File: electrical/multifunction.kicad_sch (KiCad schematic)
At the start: 19 parts

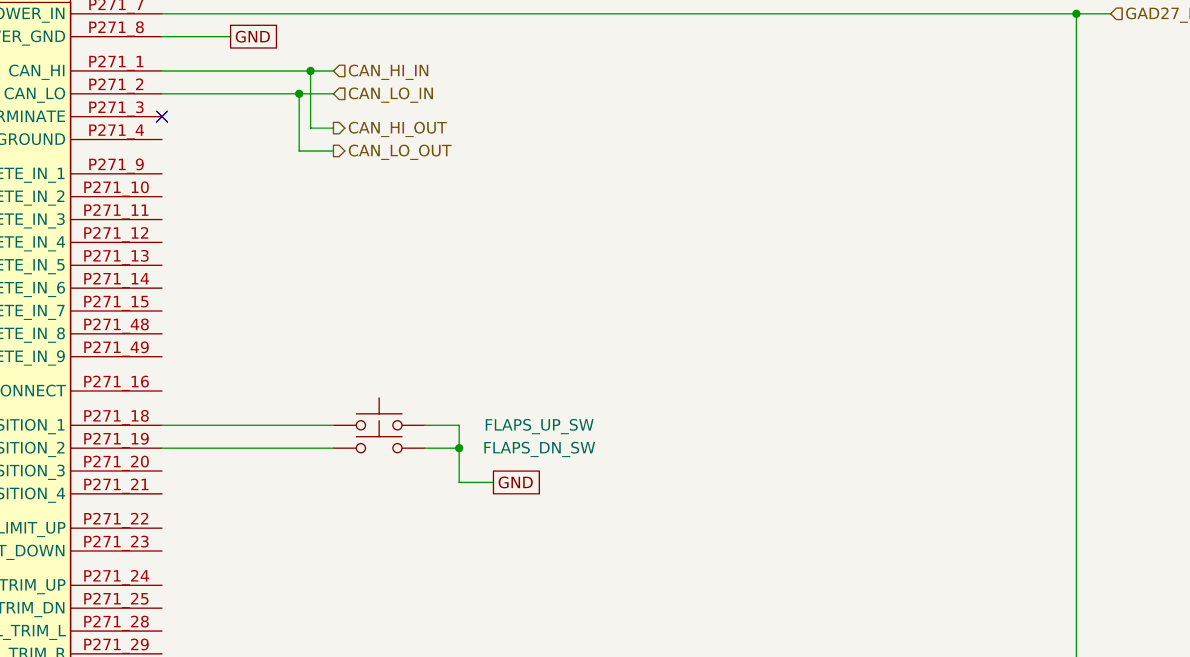
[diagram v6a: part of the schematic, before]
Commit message: Changed GTR CB to 7.5A. Added engine instrumentation. Added signal for fuel on.
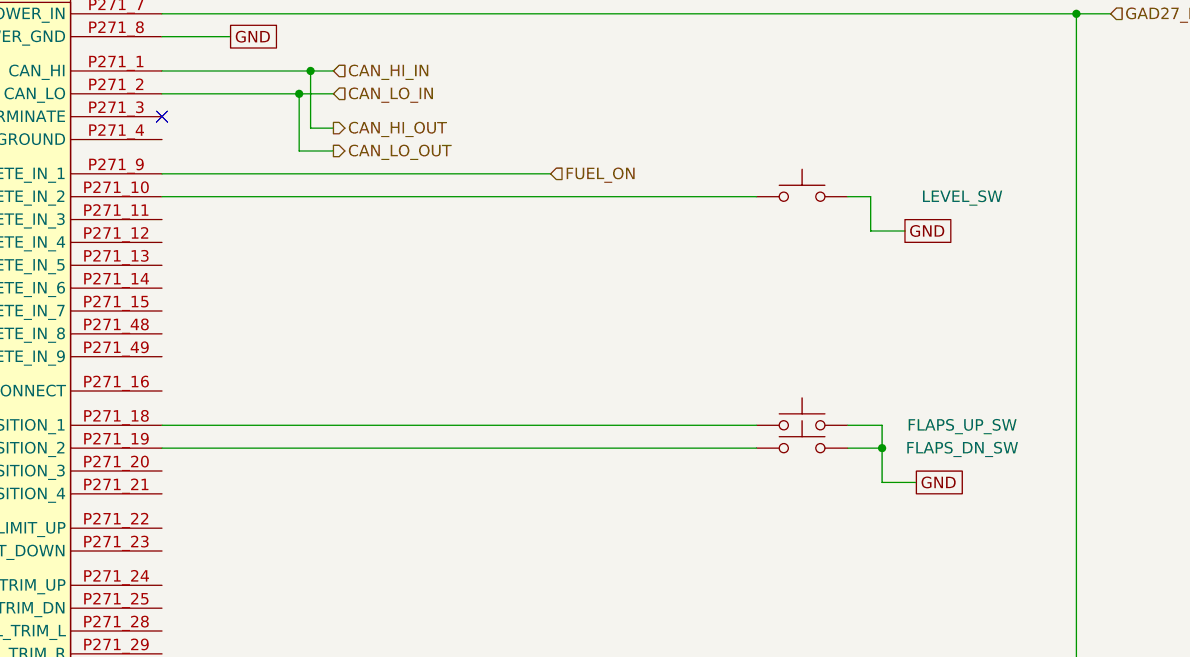
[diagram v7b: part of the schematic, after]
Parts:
- added LEVEL_SW: SW_Push, symbol Switch:SW_Push
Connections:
- net GND: now also LEVEL_SW.2
- net at GAD27.P271_10 (DISCRETE_IN_2): now also LEVEL_SW.1
- net FUEL_ON: now reaches GAD27.P271_9 (DISCRETE_IN_1)
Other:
- moved on the sheet: FLAPS_DN_SW, FLAPS_UP_SW
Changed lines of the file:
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@@
   (title_block
     (title "Flaps, Lights & Trim")
-    (date "2024-02-14")
-    (rev "0.9.3")
+    (date "2024-05-02")
+    (rev "0.9.4")
     (company "N877RV")
   )
@@
   (junction (at 110.49 213.36) (diameter 0) (color 0 0 0 0)
   )
-  (junction (at 114.3 74.93) (diameter 0) (color 0 0 0 0)
+  (junction (at 161.29 74.93) (diameter 0) (color 0 0 0 0)
   )
   (junction (at 97.79 33.02) (diameter 0) (color 0 0 0 0)
@@
   (no_connect (at 81.28 38.1))
   (no_connect (at 81.28 195.58))
-  (wire (pts (xy 81.28 74.93) (xy 100.33 74.93))
+  (wire (pts (xy 81.28 74.93) (xy 147.32 74.93))
     (stroke (width 0) (type default))
   )
@@
     (stroke (width 0) (type default))
   )
+  (wire (pts (xy 160.02 46.99) (xy 160.02 50.8))
+    (stroke (width 0) (type default))
+  )
   (wire (pts (xy 153.67 199.39) (xy 162.56 199.39))
     (stroke (width 0) (type default))
@@
     (stroke (width 0) (type default))
   )
-  (wire (pts (xy 114.3 72.39) (xy 110.49 72.39))
+  (wire (pts (xy 161.29 72.39) (xy 157.48 72.39))
     (stroke (width 0) (type default))
   )
@@
     (stroke (width 0) (type default))
   )
-  (wire (pts (xy 118.11 78.74) (xy 114.3 78.74))
+  (wire (pts (xy 165.1 78.74) (xy 161.29 78.74))
     (stroke (width 0) (type default))
   )
@@
     (stroke (width 0) (type default))
   )
-  (wire (pts (xy 81.28 72.39) (xy 100.33 72.39))
+  (wire (pts (xy 81.28 72.39) (xy 147.32 72.39))
     (stroke (width 0) (type default))
   )
@@
     (stroke (width 0) (type default))
   )
-  (wire (pts (xy 114.3 74.93) (xy 114.3 72.39))
+  (wire (pts (xy 161.29 74.93) (xy 161.29 72.39))
     (stroke (width 0) (type default))
   )
@@
     (stroke (width 0) (type default))
   )
+  (wire (pts (xy 157.48 46.99) (xy 160.02 46.99))
+    (stroke (width 0) (type default))
+  )
   (wire (pts (xy 182.88 201.93) (xy 182.88 199.39))
     (stroke (width 0) (type default))
@@
     (stroke (width 0) (type default))
   )
+  (wire (pts (xy 160.02 50.8) (xy 163.83 50.8))
+    (stroke (width 0) (type default))
+  )
   (wire (pts (xy 153.67 199.39) (xy 153.67 215.9))
     (stroke (width 0) (type default))
@@
     (stroke (width 0) (type default))
   )
+  (wire (pts (xy 81.28 46.99) (xy 147.32 46.99))
+    (stroke (width 0) (type default))
+  )
   (wire (pts (xy 153.67 181.61) (xy 153.67 199.39))
     (stroke (width 0) (type default))
@@
     (stroke (width 0) (type default))
   )
-  (wire (pts (xy 114.3 74.93) (xy 114.3 78.74))
+  (wire (pts (xy 161.29 74.93) (xy 161.29 78.74))
     (stroke (width 0) (type default))
   )
@@
     (stroke (width 0) (type default))
   )
-  (wire (pts (xy 110.49 74.93) (xy 114.3 74.93))
+  (wire (pts (xy 157.48 74.93) (xy 161.29 74.93))
+    (stroke (width 0) (type default))
+  )
+  (wire (pts (xy 81.28 44.45) (xy 124.46 44.45))
     (stroke (width 0) (type default))
   )
@@
     )
   )
-  (global_label "GND" (shape passive) (at 118.11 78.74 0) (fields_autoplaced)
-    (effects (font (size 1.27 1.27)) (justify left))
-    (property "Intersheetrefs" "${INTERSHEET_REFS}" (at 123.8544 78.74 0)
+  (global_label "GND" (shape passive) (at 165.1 78.74 0) (fields_autoplaced)
+    (effects (font (size 1.27 1.27)) (justify left))
+    (property "Intersheetrefs" "${INTERSHEET_REFS}" (at 170.8444 78.74 0)
       (effects (font (size 1.27 1.27)) (justify left) hide)
     )
@@
     )
   )
+  (global_label "GND" (shape passive) (at 163.83 50.8 0) (fields_autoplaced)
+    (effects (font (size 1.27 1.27)) (justify left))
+    (property "Intersheetrefs" "${INTERSHEET_REFS}" (at 169.5744 50.8 0)
+      (effects (font (size 1.27 1.27)) (justify left) hide)
+    )
+  )
   (global_label "GND" (shape passive) (at 40.64 243.84 0) (fields_autoplaced)
     (effects (font (size 1.27 1.27)) (justify left))
@@
   )
   (hierarchical_label "CAN_LO_IN" (shape input) (at 100.33 35.56 0) (fields_autoplaced)
+    (effects (font (size 1.27 1.27)) (justify left))
+  )
+  (hierarchical_label "FUEL_ON" (shape input) (at 124.46 44.45 0) (fields_autoplaced)
     (effects (font (size 1.27 1.27)) (justify left))
   )
@@
     )
   )
+  (symbol (lib_id "Switch:SW_Push") (at 152.4 46.99 0) (unit 1)
+    (in_bom yes) (on_board yes) (dnp no)
+    (property "Reference" "LEVEL_SW" (at 170.18 46.99 0)
+      (effects (font (size 1.27 1.27)))
+    )
+    (property "Value" "SW_Push" (at 152.4 41.91 0)
+      (effects (font (size 1.27 1.27)) hide)
+    )
+    (property "Footprint" "" (at 152.4 41.91 0)
+      (effects (font (size 1.27 1.27)) hide)
+    )
+    (property "Datasheet" "~" (at 152.4 41.91 0)
+      (effects (font (size 1.27 1.27)) hide)
+    )
+    (pin "1")
+    (pin "2")
+    (instances
+      (project "electrical"
+        (path "/e8ec215a-dbe2-4eba-a577-e50a0a128049/67540fe5-9b6d-4d8c-9d03-cde1487f48ae"
+          (reference "LEVEL_SW") (unit 1)
+        )
+      )
+    )
+  )
   (symbol (lib_id "Device:R_Potentiometer") (at 182.88 189.23 0) (mirror y) (unit 1)
     (in_bom yes) (on_board yes) (dnp no)
@@
     )
   )
-  (symbol (lib_id "Switch:SW_Push") (at 105.41 72.39 0) (unit 1)
-    (in_bom yes) (on_board yes) (dnp no)
-    (property "Reference" "FLAPS_UP_SW" (at 123.19 72.39 0)
-      (effects (font (size 1.27 1.27)))
-    )
-    (property "Value" "SW_Push" (at 105.41 67.31 0)
-      (effects (font (size 1.27 1.27)) hide)
-    )
-    (property "Footprint" "" (at 105.41 67.31 0)
-      (effects (font (size 1.27 1.27)) hide)
-    )
-    (property "Datasheet" "~" (at 105.41 67.31 0)
+  (symbol (lib_id "Switch:SW_Push") (at 152.4 72.39 0) (unit 1)
+    (in_bom yes) (on_board yes) (dnp no)
+    (property "Reference" "FLAPS_UP_SW" (at 170.18 72.39 0)
+      (effects (font (size 1.27 1.27)))
+    )
+    (property "Value" "SW_Push" (at 152.4 67.31 0)
+      (effects (font (size 1.27 1.27)) hide)
+    )
+    (property "Footprint" "" (at 152.4 67.31 0)
+      (effects (font (size 1.27 1.27)) hide)
+    )
+    (property "Datasheet" "~" (at 152.4 67.31 0)
       (effects (font (size 1.27 1.27)) hide)
     )
@@
     )
   )
-  (symbol (lib_id "Switch:SW_Push") (at 105.41 74.93 0) (unit 1)
-    (in_bom yes) (on_board yes) (dnp no)
-    (property "Reference" "FLAPS_DN_SW" (at 123.19 74.93 0)
-      (effects (font (size 1.27 1.27)))
-    )
-    (property "Value" "SW_Push" (at 105.41 69.85 0)
-      (effects (font (size 1.27 1.27)) hide)
-    )
-    (property "Footprint" "" (at 105.41 69.85 0)
-      (effects (font (size 1.27 1.27)) hide)
-    )
-    (property "Datasheet" "~" (at 105.41 69.85 0)
-      (effects (font (size 1.27 1.27)) hide)
-    )
+  (symbol (lib_id "Switch:SW_Push") (at 152.4 74.93 0) (unit 1)
+    (in_bom yes) (on_board yes) (dnp no)
+    (property "Reference" "FLAPS_DN_SW" (at 170.18 74.93 0)
+      (effects (font (size 1.27 1.27)))
+    )
+    (property "Value" "SW_Push" (at 152.4 69.85 0)
+      (effects (font (size 1.27 1.27)) hide)
+    )
+    (property "Footprint" "" (at 152.4 69.85 0)
+      (effects (font (size 1.27 1.27)) hide)
+    )
+    (property "Datasheet" "~" (at 152.4 69.85 0)
+      (effects (font (size 1.27 1.27)) hide)
+    )
